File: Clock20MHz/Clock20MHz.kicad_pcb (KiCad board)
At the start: 2 copper layers, 62.2 x 25.9 mm, 9 parts, among them J1 OUTPUT, J2 DIVIDER, U1 74AHC04, U2 74HC590A, Y1 20MHz

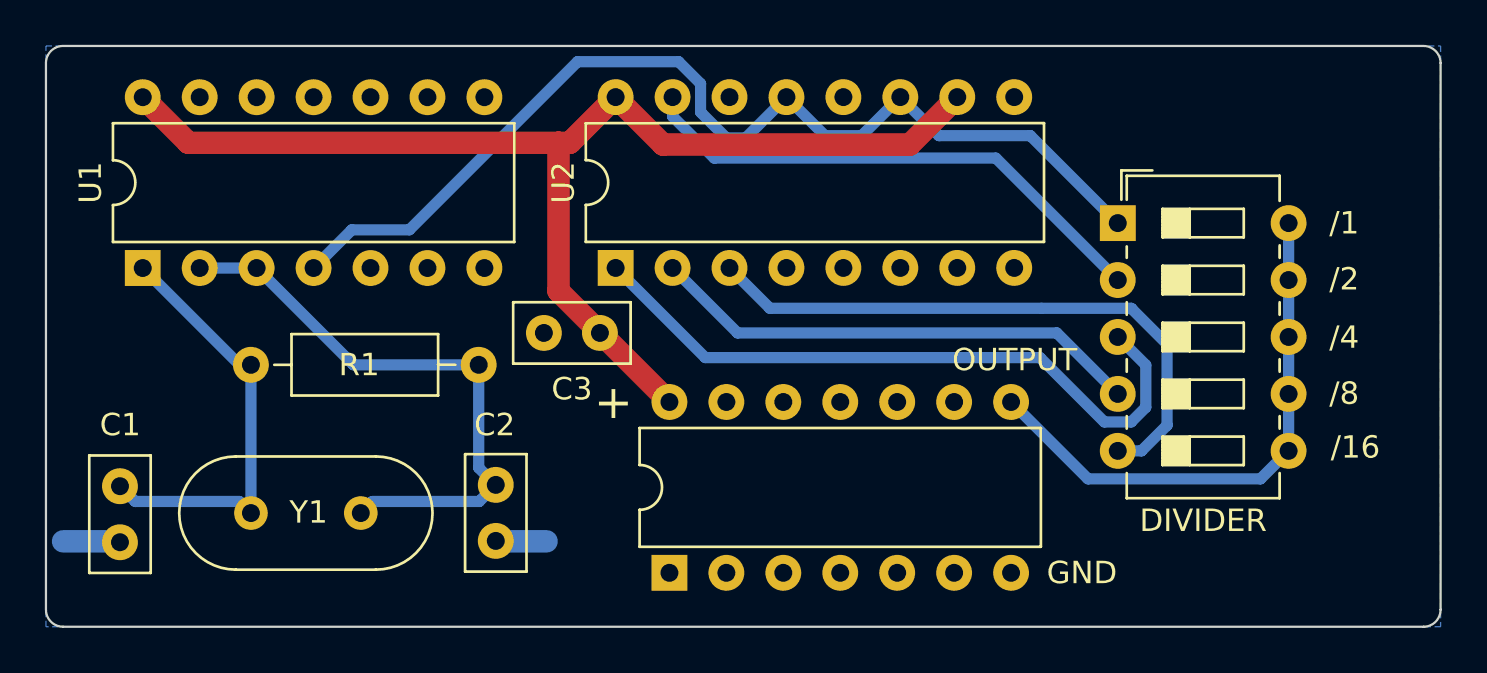
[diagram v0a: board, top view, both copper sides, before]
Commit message: Update to Kicad 6.0
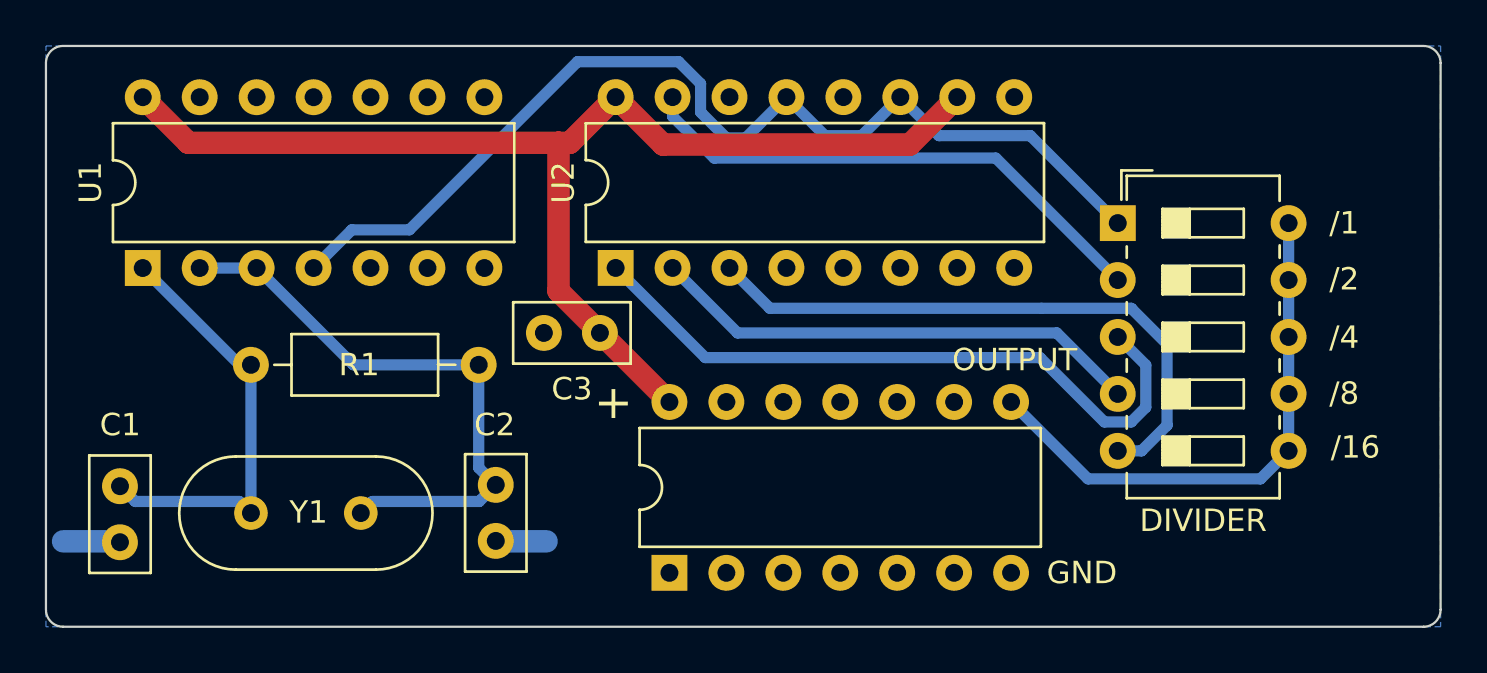
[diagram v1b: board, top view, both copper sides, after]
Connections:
- J1 pad 1: (no net) -> unconnected-(J1-Pad1)
- J1 pad 10: (no net) -> unconnected-(J1-Pad10)
- J1 pad 11: (no net) -> unconnected-(J1-Pad11)
- J1 pad 12: (no net) -> unconnected-(J1-Pad12)
- J1 pad 13: (no net) -> unconnected-(J1-Pad13)
- J1 pad 2: (no net) -> unconnected-(J1-Pad2)
- J1 pad 3: (no net) -> unconnected-(J1-Pad3)
- J1 pad 4: (no net) -> unconnected-(J1-Pad4)
- J1 pad 5: (no net) -> unconnected-(J1-Pad5)
- J1 pad 6: (no net) -> unconnected-(J1-Pad6)
- J1 pad 9: (no net) -> unconnected-(J1-Pad9)
- U1 pad 10: (no net) -> unconnected-(U1-Pad10)
- U1 pad 11: (no net) -> unconnected-(U1-Pad11)
- U1 pad 12: (no net) -> unconnected-(U1-Pad12)
- U1 pad 13: (no net) -> unconnected-(U1-Pad13)
- U1 pad 5: (no net) -> unconnected-(U1-Pad5)
- U1 pad 6: (no net) -> unconnected-(U1-Pad6)
- U1 pad 8: (no net) -> unconnected-(U1-Pad8)
- U1 pad 9: (no net) -> unconnected-(U1-Pad9)
- U2 pad 4: (no net) -> unconnected-(U2-Pad4)
- U2 pad 5: (no net) -> unconnected-(U2-Pad5)
- U2 pad 6: (no net) -> unconnected-(U2-Pad6)
- U2 pad 7: (no net) -> unconnected-(U2-Pad7)
- U2 pad 9: (no net) -> unconnected-(U2-Pad9)
